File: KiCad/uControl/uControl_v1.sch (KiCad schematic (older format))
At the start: 17 parts, among them IC1 ATMEGA328-PU, P13 AREF, P14 ANALOG_5V0, P15 ANALOG_GND, P8 FTDI, P9 ICSP, SW1 SW_PUSH, X1 CRYSTAL_2

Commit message: uControl schematic work in progress
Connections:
- net Pressure: no longer IC1.26 (PC3(ADC3))
- new net PC3_Pressure: IC1.26 (PC3(ADC3))
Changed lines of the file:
@@
-EESchema Schematic File Version 2  date 11/30/2012 11:17:28 AM
+EESchema Schematic File Version 2  date 12/1/2012 2:57:47 PM
 LIBS:uControl
 LIBS:Conn-raspberry
@@
 Sheet 1 5
 Title "uControl"
-Date "30 nov 2012"
+Date "1 dec 2012"
 Rev "1"
 Comp "WyoLum"
@@
 Comment4 ""
 $EndDescr
-Text Label 9675 3675 0    40   ~ 0
+Text Label 9600 3675 0    40   ~ 0
 IO_T
-Text Label 9675 3575 0    40   ~ 0
+Text Label 9600 3575 0    40   ~ 0
 IO_R
 Wire Wire Line
-	9675 3675 10050 3675
-Wire Wire Line
-	9675 3825 10050 3825
-Wire Wire Line
-	9675 3325 10050 3325
-Wire Wire Line
-	9675 3075 10050 3075
-Wire Wire Line
-	9675 2875 10050 2875
-Wire Wire Line
-	9675 2675 10050 2675
-Wire Wire Line
-	9675 2325 10050 2325
+	9600 3675 10050 3675
+Wire Wire Line
+	9600 3825 10050 3825
+Wire Wire Line
+	9600 3325 10050 3325
+Wire Wire Line
+	9600 3075 10050 3075
+Wire Wire Line
+	9600 2875 10050 2875
+Wire Wire Line
+	9600 2675 10050 2675
+Wire Wire Line
+	9600 2325 10050 2325
 Wire Notes Line
 	9325 625  9325 3125
 Connection ~ 5725 2625
 Wire Wire Line
-	5675 2625 5825 2625
+	5675 2625 5725 2625
+Wire Wire Line
+	5725 2625 5825 2625
 Wire Wire Line
 	5825 2625 5825 2125
@@
 	6425 2725 6375 2725
 Wire Wire Line
-	6425 2950 6425 2325
+	6425 2950 6425 2825
+Wire Wire Line
+	6425 2825 6425 2725
+Wire Wire Line
+	6425 2725 6425 2625
+Wire Wire Line
+	6425 2625 6425 2525
+Wire Wire Line
+	6425 2525 6425 2425
+Wire Wire Line
+	6425 2425 6425 2325
 Wire Wire Line
 	6425 2325 6375 2325
@@
 	5725 2425 5675 2425
 Wire Wire Line
-	5725 2125 5725 2525
-Wire Wire Line
-	5725 2625 5725 2825
+	5725 2125 5725 2325
+Wire Wire Line
+	5725 2325 5725 2425
+Wire Wire Line
+	5725 2425 5725 2525
+Wire Wire Line
+	5725 2625 5725 2725
+Wire Wire Line
+	5725 2725 5725 2825
 Wire Wire Line
 	5725 2825 5675 2825
@@
 	875  3300 825  3300
 Wire Wire Line
-	825  3300 825  2800
+	825  3300 825  3050
+Wire Wire Line
+	825  3050 825  2800
 Wire Wire Line
 	825  2800 875  2800
 Connection ~ 1400 2800
 Wire Wire Line
-	1275 2800 1925 2800
-Wire Wire Line
-	1800 1650 1800 4975
+	1275 2800 1400 2800
+Wire Wire Line
+	1400 2800 1925 2800
+Wire Wire Line
+	1800 1650 1800 2450
+Wire Wire Line
+	1800 2450 1800 4975
 Wire Notes Line
 	5400 7750 5400 6325
@@
 	4750 7275 4750 6450
 Wire Wire Line
-	4550 6450 4550 7275
+	4550 6450 4550 7150
+Wire Wire Line
+	4550 7150 4550 7275
 Wire Wire Line
 	4950 7275 4950 6450
@@
 	6675 2525 6525 2525
 Wire Wire Line
-	2900 5100 2900 4850
+	2900 5100 2900 4975
+Wire Wire Line
+	2900 4975 2900 4850
 Wire Wire Line
 	8575 2825 8825 2825
@@
 	9675 6150 10050 6150
 Wire Wire Line
-	6425 1825 6675 1825
+	6425 1825 6625 1825
+Wire Wire Line
+	6625 1825 6675 1825
 Wire Wire Line
 	3900 3350 4125 3350
@@
 	3900 3650 4125 3650
 Wire Wire Line
-	1400 800  4800 800
-Wire Wire Line
-	4800 650  4800 1200
+	1400 800  1575 800
+Wire Wire Line
+	1575 800  1800 800
+Wire Wire Line
+	1800 800  2900 800
+Wire Wire Line
+	2900 800  4600 800
+Wire Wire Line
+	4600 800  4800 800
+Wire Wire Line
+	4800 650  4800 800
+Wire Wire Line
+	4800 800  4800 1200
 Wire Wire Line
 	6675 1625 6425 1625
 Wire Wire Line
-	6675 1925 6425 1925
+	6675 1925 6625 1925
+Wire Wire Line
+	6625 1925 6425 1925
 Wire Wire Line
 	9675 6350 10050 6350
@@
 	6675 2825 6525 2825
 Wire Wire Line
-	1575 4050 1575 1700
+	1575 4050 1575 2250
+Wire Wire Line
+	1575 2250 1575 1700
 Connection ~ 1575 2250
 Wire Wire Line
@@
 Connection ~ 1800 2450
 Wire Wire Line
-	1925 3300 1275 3300
+	1925 3300 1400 3300
+Wire Wire Line
+	1400 3300 1275 3300
 Connection ~ 1400 3300
 Wire Wire Line
@@
 	750  3050 750  4975
 Wire Wire Line
-	750  4975 2900 4975
+	750  4975 1575 4975
+Wire Wire Line
+	1575 4975 1800 4975
+Wire Wire Line
+	1800 4975 2900 4975
 Connection ~ 1575 4975
 Wire Wire Line
@@
 	5100 3125 5100 625
 Wire Wire Line
-	9675 2425 10050 2425
-Wire Wire Line
-	9675 2775 10050 2775
-Wire Wire Line
-	9675 2975 10050 2975
-Wire Wire Line
-	9675 3225 10050 3225
-Wire Wire Line
-	9675 3475 10050 3475
-Wire Wire Line
-	9675 3975 10050 3975
-Wire Wire Line
-	10050 3575 9675 3575
-Text Label 9675 2325 0    40   ~ 0
+	9600 2425 10050 2425
+Wire Wire Line
+	9600 2775 10050 2775
+Wire Wire Line
+	9600 2975 10050 2975
+Wire Wire Line
+	9600 3225 10050 3225
+Wire Wire Line
+	9600 3475 10050 3475
+Wire Wire Line
+	9600 3975 10050 3975
+Wire Wire Line
+	10050 3575 9600 3575
+Text Label 9600 2325 0    40   ~ 0
 V_IN
-Text Label 9675 2425 0    40   ~ 0
+Text Label 9600 2425 0    40   ~ 0
 5V0
-Text Label 9675 2675 0    40   ~ 0
+Text Label 9600 2675 0    40   ~ 0
 ~MOSI
-Text Label 9675 2775 0    40   ~ 0
+Text Label 9600 2775 0    40   ~ 0
 ~SS
-Text Label 9675 2875 0    40   ~ 0
+Text Label 9600 2875 0    40   ~ 0
 SCK
-Text Label 9675 2975 0    40   ~ 0
+Text Label 9600 2975 0    40   ~ 0
 MISO
-Text Label 9675 3075 0    40   ~ 0
-Pressure
-Text Label 9675 3225 0    40   ~ 0
+Text Label 9600 3075 0    40   ~ 0
+PC3_Pressure
+Text Label 9600 3225 0    40   ~ 0
 ~Flow_Tx
-Text Label 9675 3325 0    40   ~ 0
+Text Label 9600 3325 0    40   ~ 0
 Flow_Rx
-Text Label 9675 3475 0    40   ~ 0
+Text Label 9600 3475 0    40   ~ 0
 IO_X
-Text Label 9675 3825 0    40   ~ 0
+Text Label 9600 3825 0    40   ~ 0
 ~Valve
-Text Label 9675 3975 0    40   ~ 0
+Text Label 9600 3975 0    40   ~ 0
 GND
 $Sheet
@@
 F2 "SCK" I L 10050 2875 60
 F3 "MISO" I L 10050 2975 60
-F4 "Pressure" I L 10050 3075 60
-F5 "V_IN" I L 10050 2325 60
-F6 "Flow_Rx" O L 10050 3325 60
-F7 "GND" B L 10050 3975 60
-F8 "5V0" B L 10050 2425 60
-F9 "~Valve" I L 10050 3825 60
-F10 "~Flow_Tx" I L 10050 3225 60
-F11 "~MOSI" I L 10050 2675 60
-F12 "~SS" I L 10050 2775 60
-F13 "IO_T" O L 10050 3675 60
-F14 "IO_R" I L 10050 3575 60
-F15 "IO_X" I L 10050 3475 60
+F4 "V_IN" I L 10050 2325 60
+F5 "Flow_Rx" O L 10050 3325 60
+F6 "GND" B L 10050 3975 60
+F7 "5V0" B L 10050 2425 60
+F8 "~Valve" I L 10050 3825 60
+F9 "~Flow_Tx" I L 10050 3225 60
+F10 "~MOSI" I L 10050 2675 60
+F11 "~SS" I L 10050 2775 60
+F12 "IO_T" O L 10050 3675 60
+F13 "IO_R" I L 10050 3575 60
+F14 "IO_X" I L 10050 3475 60
+F15 "PC3_Pressure" I L 10050 3075 60
 $EndSheet
 Text Label 5825 2125 0    40   ~ 0
@@
 PC2
 Text Label 4125 2550 0    40   ~ 0
-Pressure
+PC3_Pressure
 Text Label 4125 3150 0    40   ~ 0
 RXD

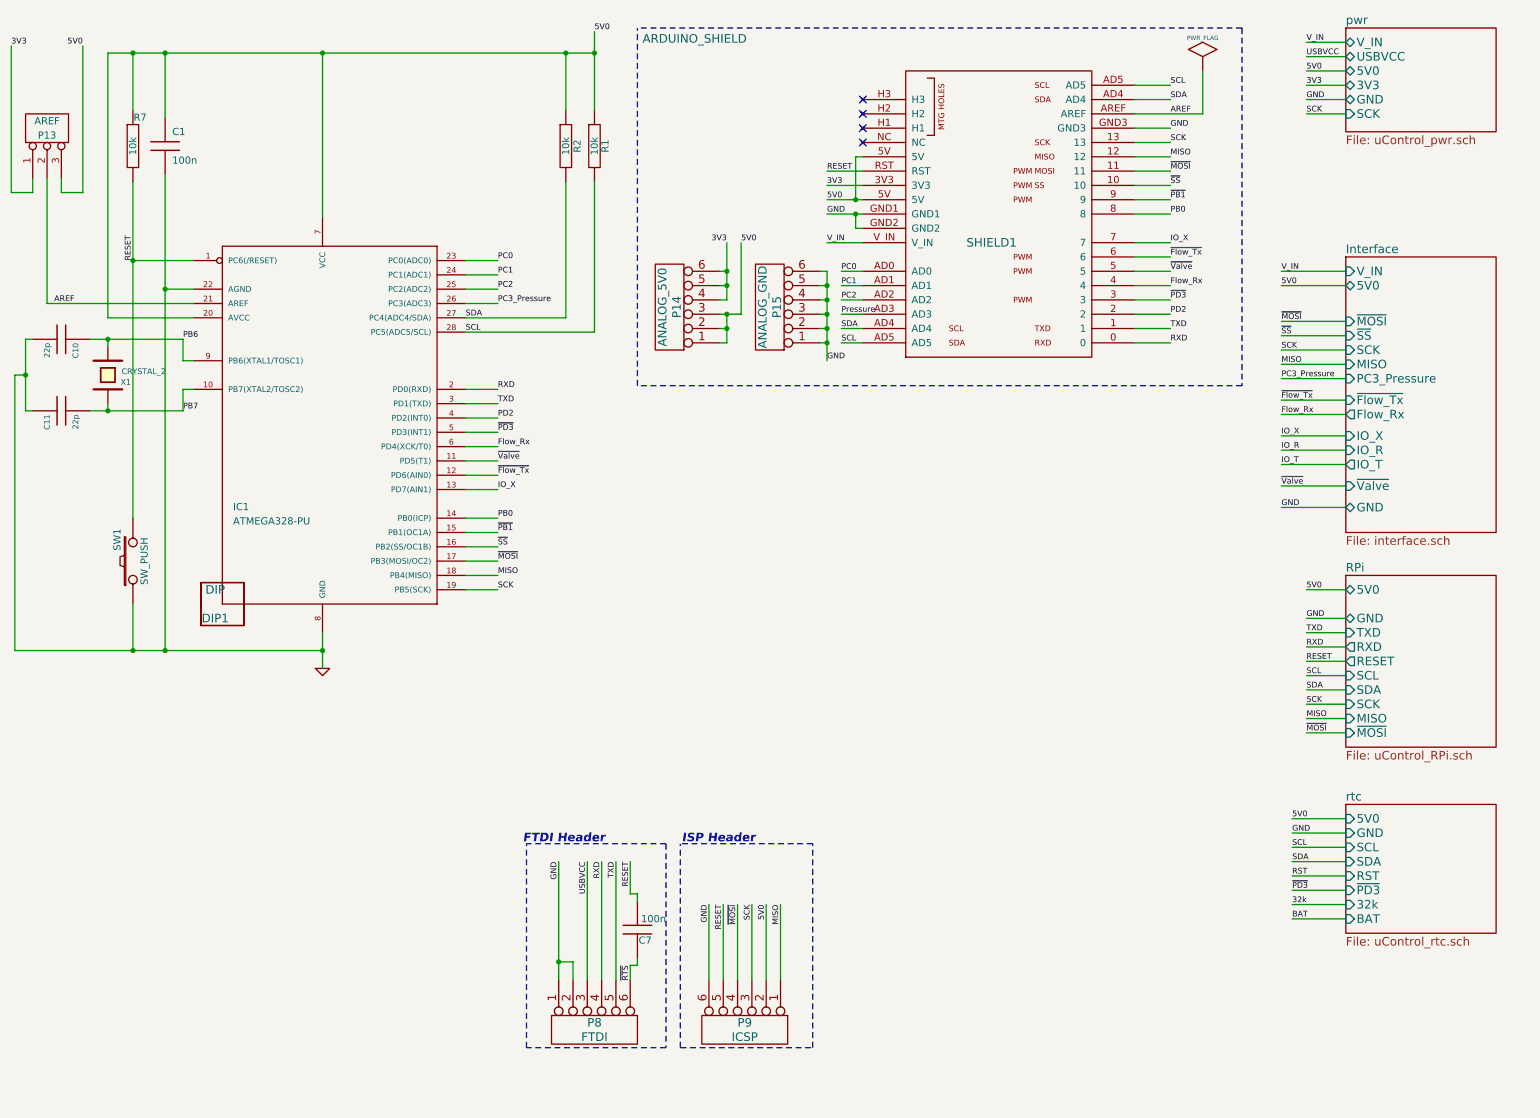
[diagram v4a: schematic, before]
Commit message: uControl : added Temp and Pulse sensors. P/N's for Diodes, Transistor etc.
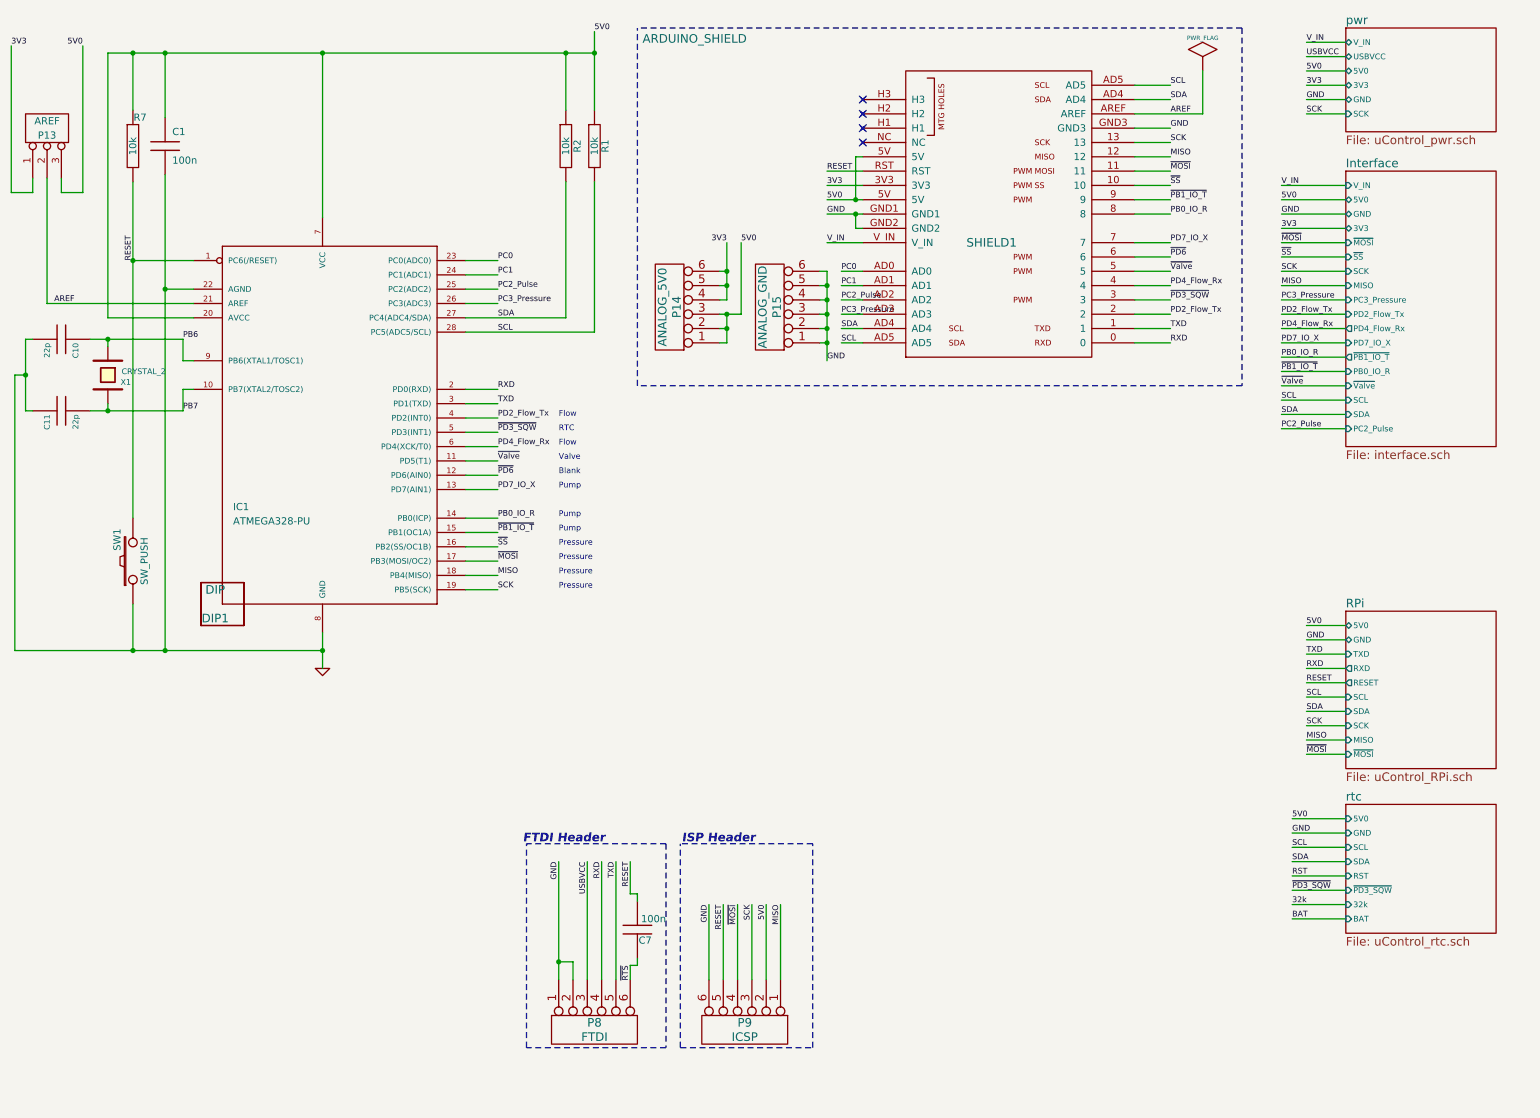
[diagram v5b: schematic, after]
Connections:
- net Pressure is gone; now on net PC3_Pressure: SHIELD1.AD3
- net Flow_Rx renamed PD4_Flow_Rx
- net IO_X renamed PD7_IO_X
- net PB0 renamed PB0_IO_R
- net PC2 renamed PC2_Pulse
- net PD2 renamed PD2_Flow_Tx
- net ~Flow_Tx renamed ~PD6
- net ~PB1 renamed ~PB1_IO_T
- net ~PD3 renamed ~PD3_SQW
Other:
- note added: "Blank"
- note added: "Flow"
- note added: "Pressure"
- note added: "Pump"
- note added: "RTC"
- note added: "Valve"

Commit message: uControl schematic work in progress
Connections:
- net ~Valve: no longer IC1.11 (PD5(T1))
- new net ~PD5_Valve: IC1.11 (PD5(T1))
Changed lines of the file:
@@
-EESchema Schematic File Version 2  date Sunday 02 December 2012 02:01:49 AM IST
+EESchema Schematic File Version 2  date Sunday 02 December 2012 11:21:38 PM IST
 LIBS:uControl
 LIBS:Conn-raspberry
@@
 Sheet 1 5
 Title "uControl"
-Date "1 dec 2012"
+Date "2 dec 2012"
 Rev "1"
 Comp "WyoLum"
@@
 F5 "GND" B L 10050 1925 40
 F6 "5V0" B L 10050 1825 40
-F7 "~Valve" I L 10050 3125 40
+F7 "~PD5_Valve" I L 10050 3125 40
 F8 "~MOSI" I L 10050 2125 40
 F9 "~SS" I L 10050 2225 40
@@
 PD7_IO_X
 Text Label 9600 3125 0    40   ~ 0
-~Valve
+~PD5_Valve
 Text Label 9600 1925 0    40   ~ 0
 GND
@@
 RESET
 Text Label 4125 3650 0    40   ~ 0
-~Valve
+~PD5_Valve
 Text Label 4125 3750 0    40   ~ 0
 ~PD6

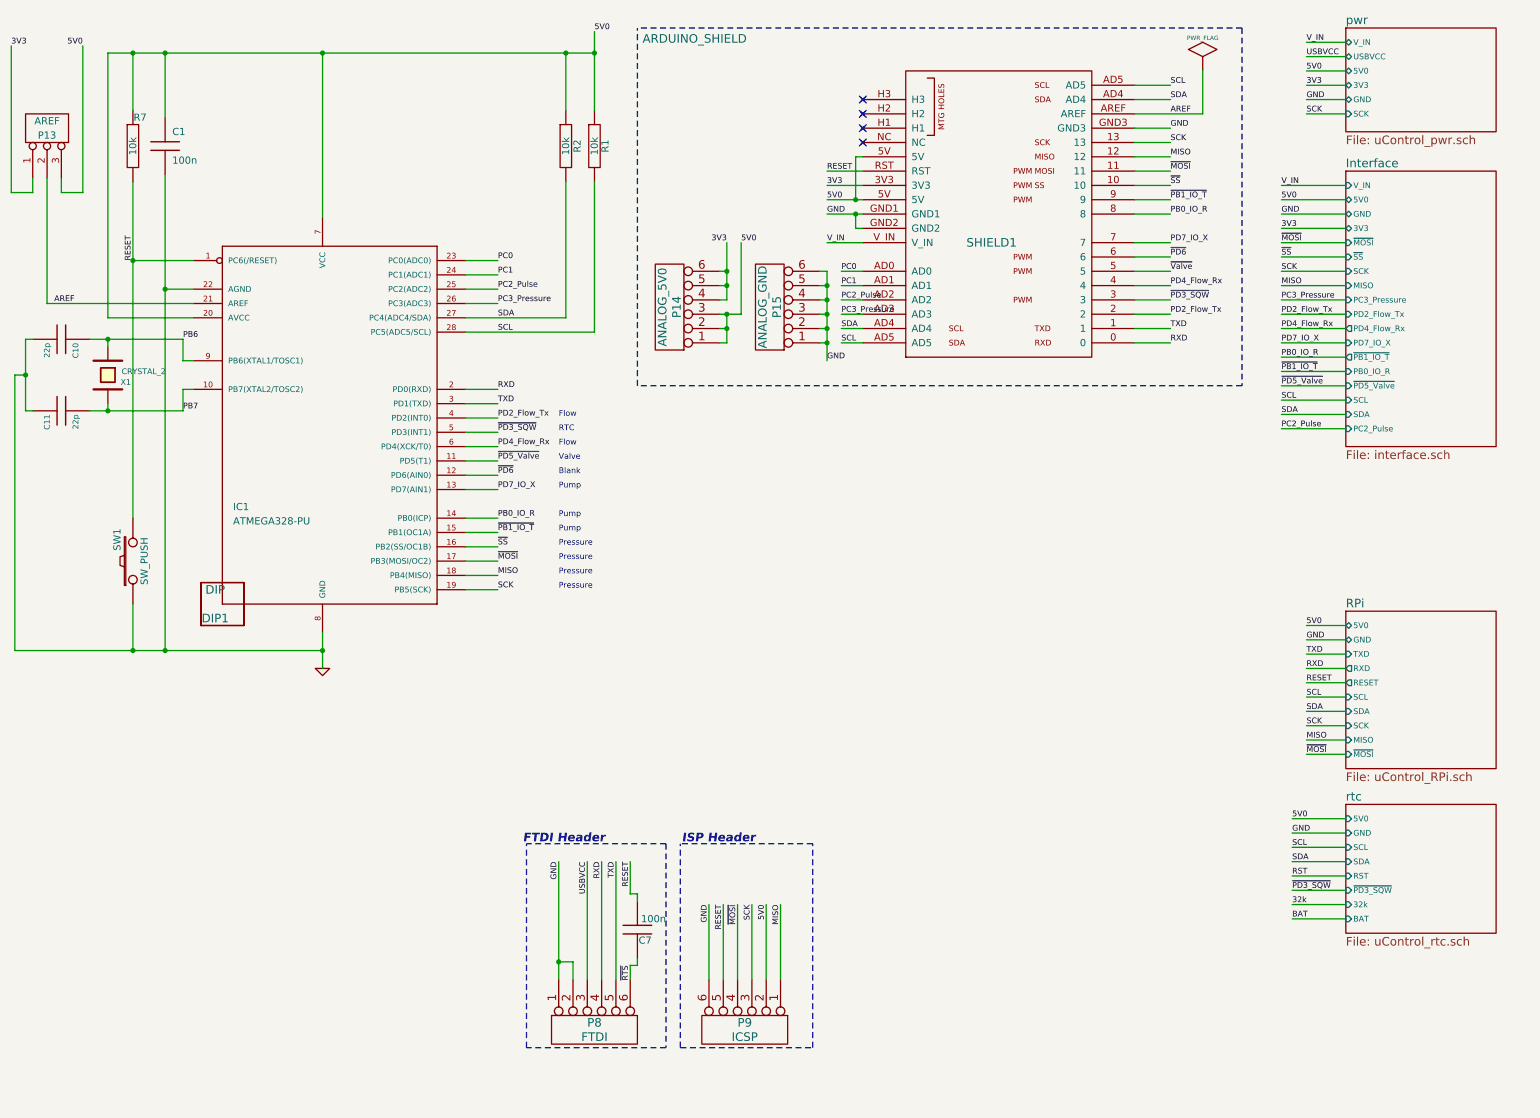
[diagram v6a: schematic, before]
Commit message: uControl schematic work in progress. Added #2 Pr Sensor. Renamed V_In to 12V
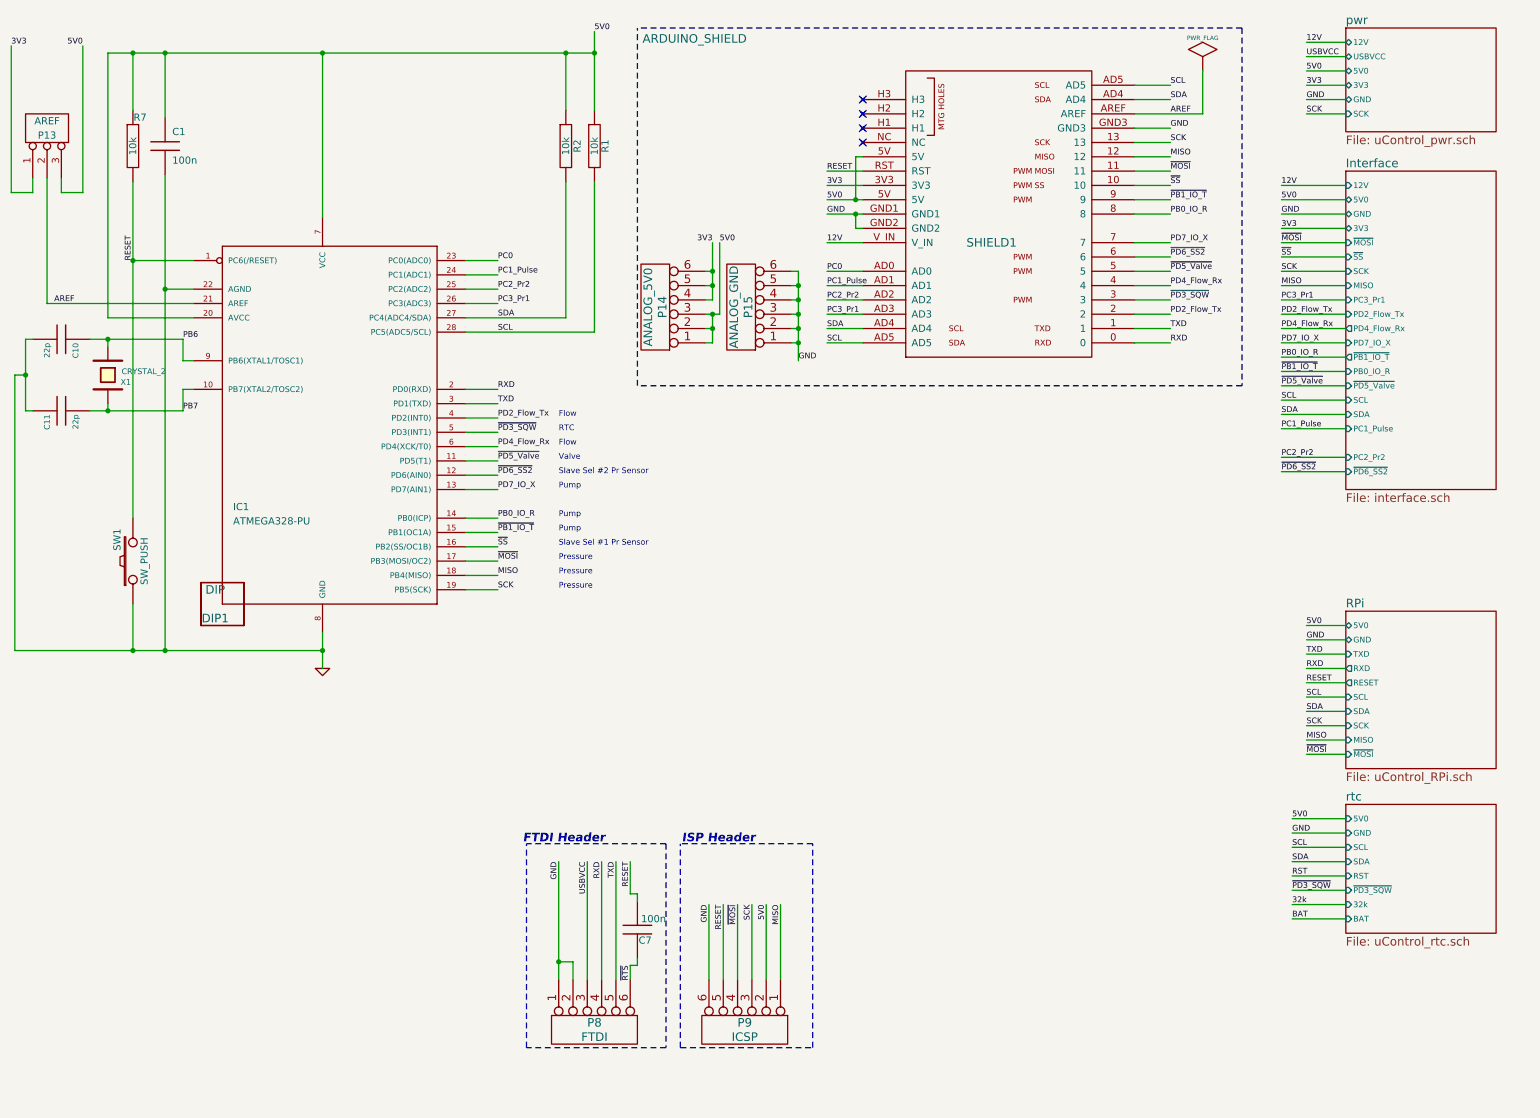
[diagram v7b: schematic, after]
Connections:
- net ~Valve is gone; now on net ~PD5_Valve: SHIELD1.5
- net PC1 renamed PC1_Pulse
- net PC2_Pulse renamed PC2_Pr2
- net PC3_Pressure renamed PC3_Pr1
- net V_IN renamed 12V
- net ~PD6 renamed ~PD6_SS2
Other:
- note added: "Slave Sel #1 Pr Sensor"
- note added: "Slave Sel #2 Pr Sensor"
- note removed: "Blank"
- moved on the sheet: P14, P15

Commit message: uControl some minor edits to schematic
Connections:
- net USBVCC: no longer P8.3
- no-connect marks 4 -> 5
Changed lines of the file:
@@
-EESchema Schematic File Version 2  date 12/5/2012 11:54:40 AM
+EESchema Schematic File Version 2  date 12/6/2012 4:59:12 PM
 LIBS:uControl
 LIBS:Conn-raspberry
@@
 Sheet 1 5
 Title "uControl"
-Date "5 dec 2012"
+Date "6 dec 2012"
 Rev "1"
 Comp "WyoLum"
@@
 Comment4 ""
 $EndDescr
+NoConn ~ 4750 7275
 Text Label 9600 3725 0    40   ~ 0
 ~PD6_SS2
@@
 Wire Wire Line
 	6100 7275 6100 6750
-Wire Wire Line
-	4750 7275 4750 6450
 Wire Wire Line
 	4550 6450 4550 7150
@@
 Text Label 5600 6750 3    40   ~ 0
 GND
-Text Label 4750 6450 3    40   ~ 0
-USBVCC
 Text Label 6100 6750 3    40   ~ 0
 MISO
